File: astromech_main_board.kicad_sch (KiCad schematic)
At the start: 0 parts

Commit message: added blocks
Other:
- added sheet ESP32 (ESP32.kicad_sch)
- added sheet io_expander (io_expander.kicad_sch)
- added sheet io_protection (io_protection.kicad_sch)
- added sheet power_protection (power_protection.kicad_sch)
- added sheet voltage_monitoring (voltage_monitoring.kicad_sch)
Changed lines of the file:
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@@
 	(generator_version "8.0")
 	(paper "A4")
+	(sheet
+		(at 172.72 121.92)
+		(size 34.29 27.94)
+		(fields_autoplaced yes)
+		(stroke
+			(width 0.1524)
+			(type solid)
+		)
+		(fill
+			(color 0 0 0 0.0000)
+		)
+		(property "Sheetname" "io_protection"
+			(at 172.72 121.2084 0)
+			(effects
+				(font
+					(size 1.27 1.27)
+				)
+				(justify left bottom)
+			)
+		)
+		(property "Sheetfile" "io_protection.kicad_sch"
+			(at 172.72 150.4446 0)
+			(effects
+				(font
+					(size 1.27 1.27)
+				)
+				(justify left top)
+			)
+		)
+		(instances
+			(project "astromech_main_board"
+				(path "/3ed70c37-1dc6-4761-9813-fca49ce12494"
+					(page "6")
+				)
+			)
+		)
+	)
+	(sheet
+		(at 115.57 128.27)
+		(size 39.37 35.56)
+		(fields_autoplaced yes)
+		(stroke
+			(width 0.1524)
+			(type solid)
+		)
+		(fill
+			(color 0 0 0 0.0000)
+		)
+		(property "Sheetname" "io_expander"
+			(at 115.57 127.5584 0)
+			(effects
+				(font
+					(size 1.27 1.27)
+				)
+				(justify left bottom)
+			)
+		)
+		(property "Sheetfile" "io_expander.kicad_sch"
+			(at 115.57 164.4146 0)
+			(effects
+				(font
+					(size 1.27 1.27)
+				)
+				(justify left top)
+			)
+		)
+		(instances
+			(project "astromech_main_board"
+				(path "/3ed70c37-1dc6-4761-9813-fca49ce12494"
+					(page "5")
+				)
+			)
+		)
+	)
+	(sheet
+		(at 45.72 109.22)
+		(size 35.56 30.48)
+		(fields_autoplaced yes)
+		(stroke
+			(width 0.1524)
+			(type solid)
+		)
+		(fill
+			(color 0 0 0 0.0000)
+		)
+		(property "Sheetname" "power_protection"
+			(at 45.72 108.5084 0)
+			(effects
+				(font
+					(size 1.27 1.27)
+				)
+				(justify left bottom)
+			)
+		)
+		(property "Sheetfile" "power_protection.kicad_sch"
+			(at 45.72 140.2846 0)
+			(effects
+				(font
+					(size 1.27 1.27)
+				)
+				(justify left top)
+			)
+		)
+		(instances
+			(project "astromech_main_board"
+				(path "/3ed70c37-1dc6-4761-9813-fca49ce12494"
+					(page "4")
+				)
+			)
+		)
+	)
+	(sheet
+		(at 125.73 66.04)
+		(size 34.29 48.26)
+		(fields_autoplaced yes)
+		(stroke
+			(width 0.1524)
+			(type solid)
+		)
+		(fill
+			(color 0 0 0 0.0000)
+		)
+		(property "Sheetname" "ESP32"
+			(at 125.73 65.3284 0)
+			(effects
+				(font
+					(size 1.27 1.27)
+				)
+				(justify left bottom)
+			)
+		)
+		(property "Sheetfile" "ESP32.kicad_sch"
+			(at 125.73 114.8846 0)
+			(effects
+				(font
+					(size 1.27 1.27)
+				)
+				(justify left top)
+			)
+		)
+		(instances
+			(project "astromech_main_board"
+				(path "/3ed70c37-1dc6-4761-9813-fca49ce12494"
+					(page "2")
+				)
+			)
+		)
+	)
+	(sheet
+		(at 45.72 55.88)
+		(size 30.48 30.48)
+		(fields_autoplaced yes)
+		(stroke
+			(width 0.1524)
+			(type solid)
+		)
+		(fill
+			(color 0 0 0 0.0000)
+		)
+		(property "Sheetname" "voltage_monitoring"
+			(at 45.72 55.1684 0)
+			(effects
+				(font
+					(size 1.27 1.27)
+				)
+				(justify left bottom)
+			)
+		)
+		(property "Sheetfile" "voltage_monitoring.kicad_sch"
+			(at 45.72 86.9446 0)
+			(effects
+				(font
+					(size 1.27 1.27)
+				)
+				(justify left top)
+			)
+		)
+		(instances
+			(project "astromech_main_board"
+				(path "/3ed70c37-1dc6-4761-9813-fca49ce12494"
+					(page "3")
+				)
+			)
+		)
+	)
 	(sheet_instances
 		(path "/"

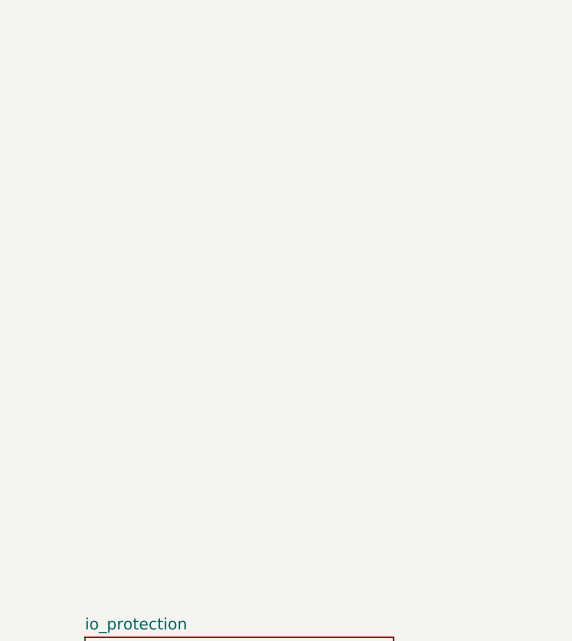
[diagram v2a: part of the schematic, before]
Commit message: added hw encoder
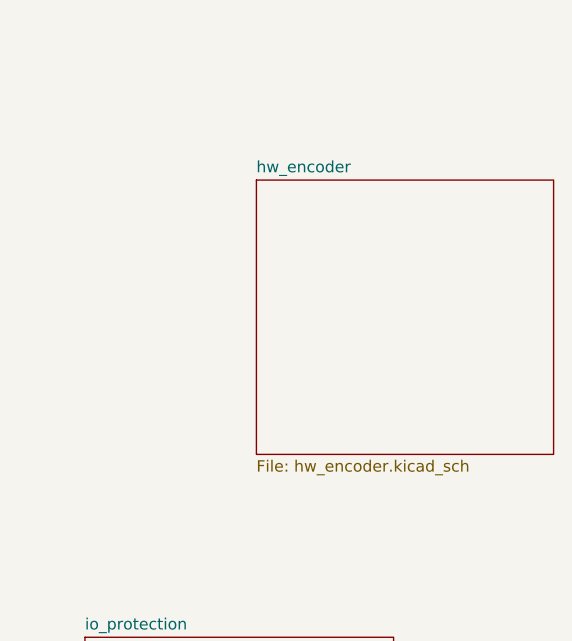
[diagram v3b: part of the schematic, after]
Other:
- added sheet hw_encoder (hw_encoder.kicad_sch)
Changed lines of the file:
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@@
 	(paper "A4")
+	(sheet
+		(at 191.77 71.12)
+		(size 33.02 30.48)
+		(fields_autoplaced yes)
+		(stroke
+			(width 0.1524)
+			(type solid)
+		)
+		(fill
+			(color 0 0 0 0.0000)
+		)
+		(property "Sheetname" "hw_encoder"
+			(at 191.77 70.4084 0)
+			(effects
+				(font
+					(size 1.27 1.27)
+				)
+				(justify left bottom)
+			)
+		)
+		(property "Sheetfile" "hw_encoder.kicad_sch"
+			(at 191.77 102.1846 0)
+			(effects
+				(font
+					(size 1.27 1.27)
+				)
+				(justify left top)
+			)
+		)
+		(instances
+			(project "astromech_main_board"
+				(path "/3ed70c37-1dc6-4761-9813-fca49ce12494"
+					(page "7")
+				)
+			)
+		)
+	)
 	(sheet
 		(at 172.72 121.92)

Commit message: moved power protection
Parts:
- added C1, C3: 0.1u, symbol Device:C_Polarized_Small
- added C2: C_Polarized, symbol Device:C_Polarized
- added F1, F2: ??A, symbol Device:Fuse_Small
- added J1, J2: Screw_Terminal_01x02, symbol Connector:Screw_Terminal_01x02
- added JP10, JP11, JP9: SolderJumper_3_Open, symbol Jumper:SolderJumper_3_Open
- added U7, U9: NCP1117-5.0_TO252, Package_TO_SOT_SMD:TO-252-2, symbol Regulator_Linear:NCP1117-5.0_TO252
- added U8: NCP1117-3.3_SOT223, Package_TO_SOT_SMD:SOT-223-3_TabPin2, symbol Regulator_Linear:NCP1117-3.3_SOT223
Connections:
- new net: JP10.1 (A), U7.2 (VO)
- new net: JP10.3 (B), U7.3 (VI)
- new net: F2.1, J2.1 (Pin_1)
- new net: JP11.3 (B), U8.3 (VI)
- new net: JP9.3 (B), U9.3 (VI)
- new net: F1.1, J1.1 (Pin_1)
- new net 3V3_IN: C3.1, F1.2, JP11.2 (C)
- new net 3V3_REG: JP11.1 (A), U8.2 (VO)
- new net 5V_IN: C1.1, F2.2, JP9.2 (C)
- new net 5V_REG: JP9.1 (A), U9.2 (VO)
- new net GND: C1.2, C2.2, C3.2, J1.2 (Pin_2), J2.2 (Pin_2), U7.1 (GND), U8.1 (GND), U9.1 (GND)
- new net VCC: C2.1, JP10.2 (C)
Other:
- removed sheet power_protection
- sheet ESP32 ports: added 3V3_IN, 5Vin, DPAD_CENTER, DPAD_COM, DPAD_DOWN, DPAD_LEFT, DPAD_RIGHT, DPAD_UP, ENC_HEAD_CS, ENC_HEAD_PICO, ENC_HEAD_POCI, ENC_HEAD_SCK, ENC_LEFT_CS, ENC_LEFT_PICO, ENC_LEFT_POCI, ENC_LEFT_SCK, ENC_RIGHT_CS, ENC_RIGHT_PICO, ENC_RIGHT_POCI, ENC_RIGHT_SCK, GND, I2C_SCL, I2C_SDA, PWM_HEAD, PWM_LEFT, PWM_RIGHT, SCREEN_CS, SCREEN_PICO, SCREEN_POCI, SCREEN_SCK, UART_GP_RX, UART_GP_TX, UART_RC_RX, UART_RC_TX, UI_HEARTBEAT, UI_POWER; removed none
- note added: "5.0 Voltage Input"
- note added: "Non-Regualted Voltage"
- note added: "Output Voltage"
- note added: "Regulated Voltage"

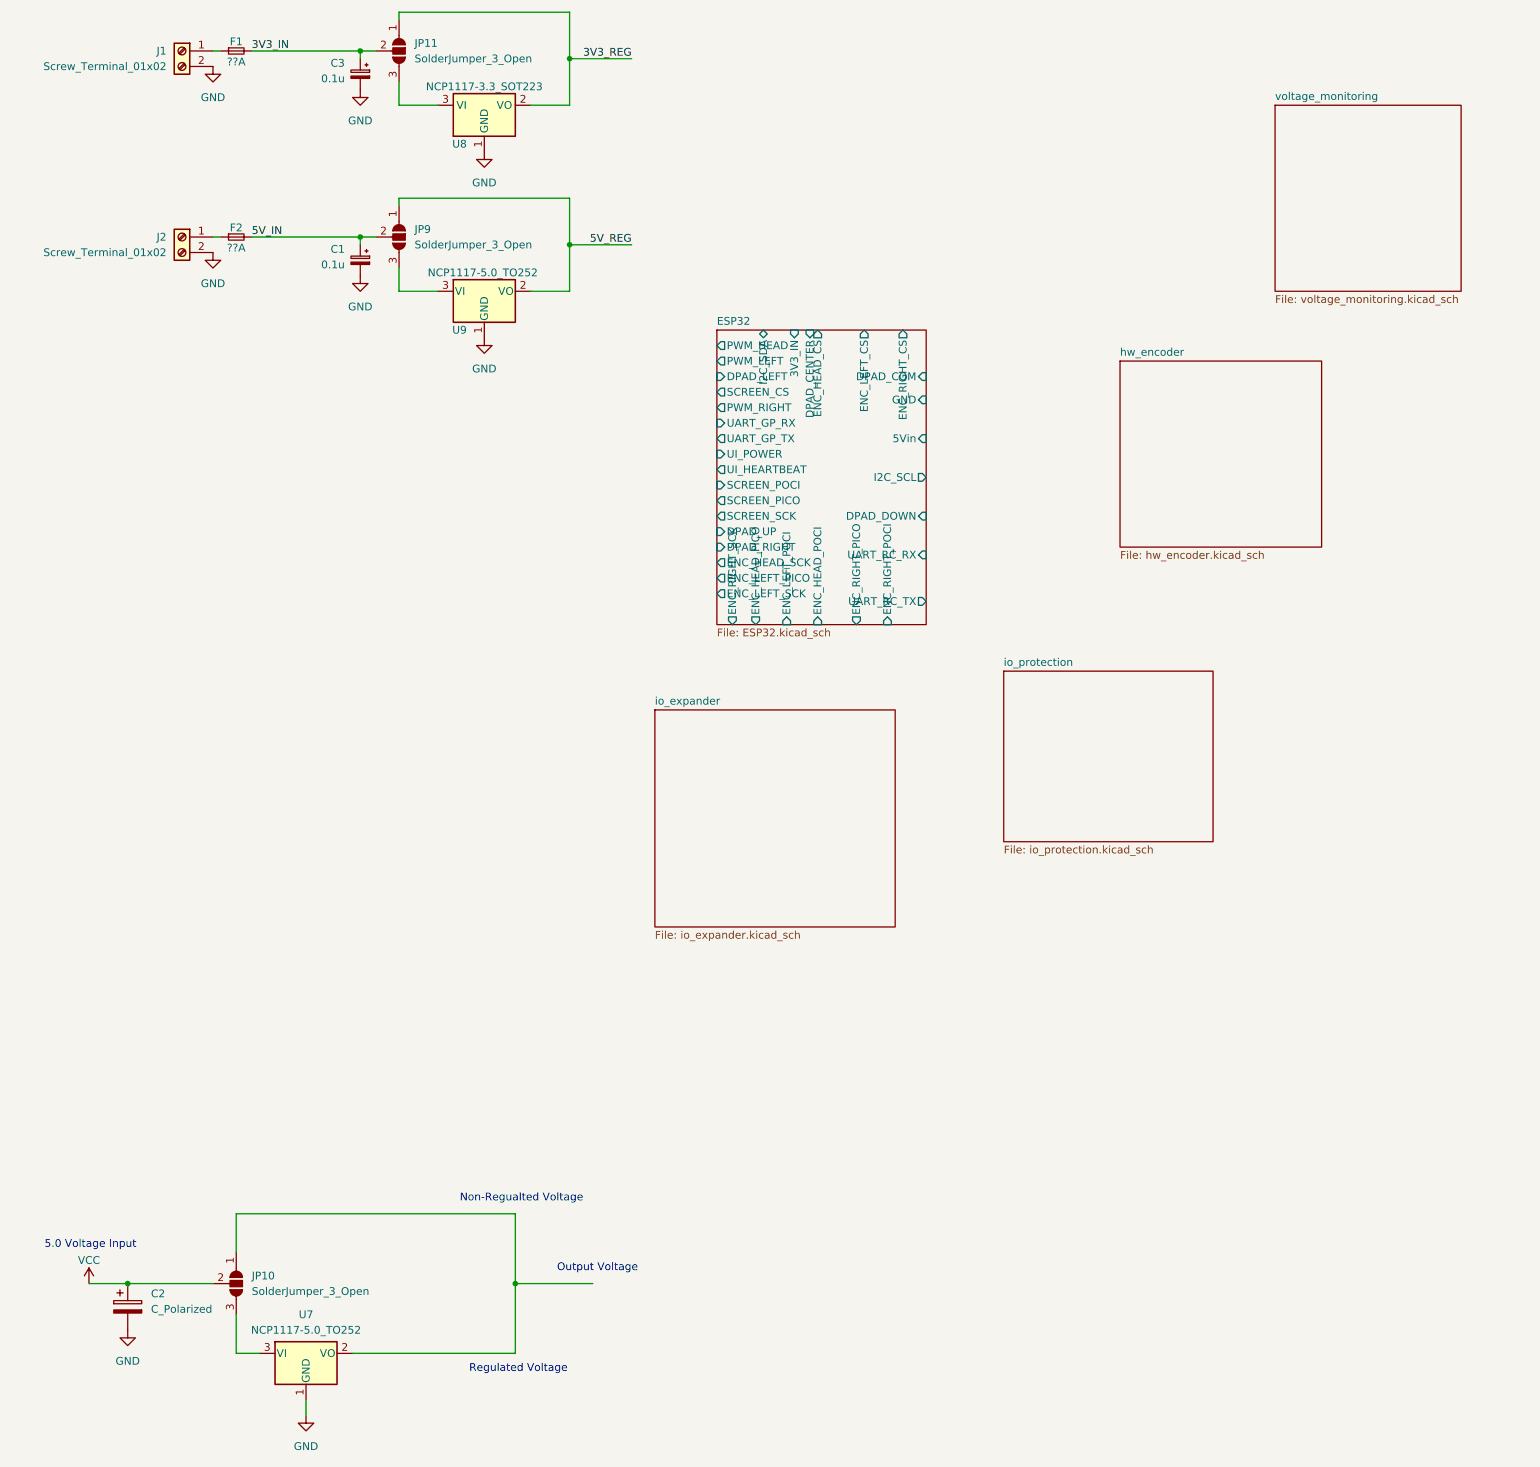
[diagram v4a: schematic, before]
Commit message: moved voltage monitoring
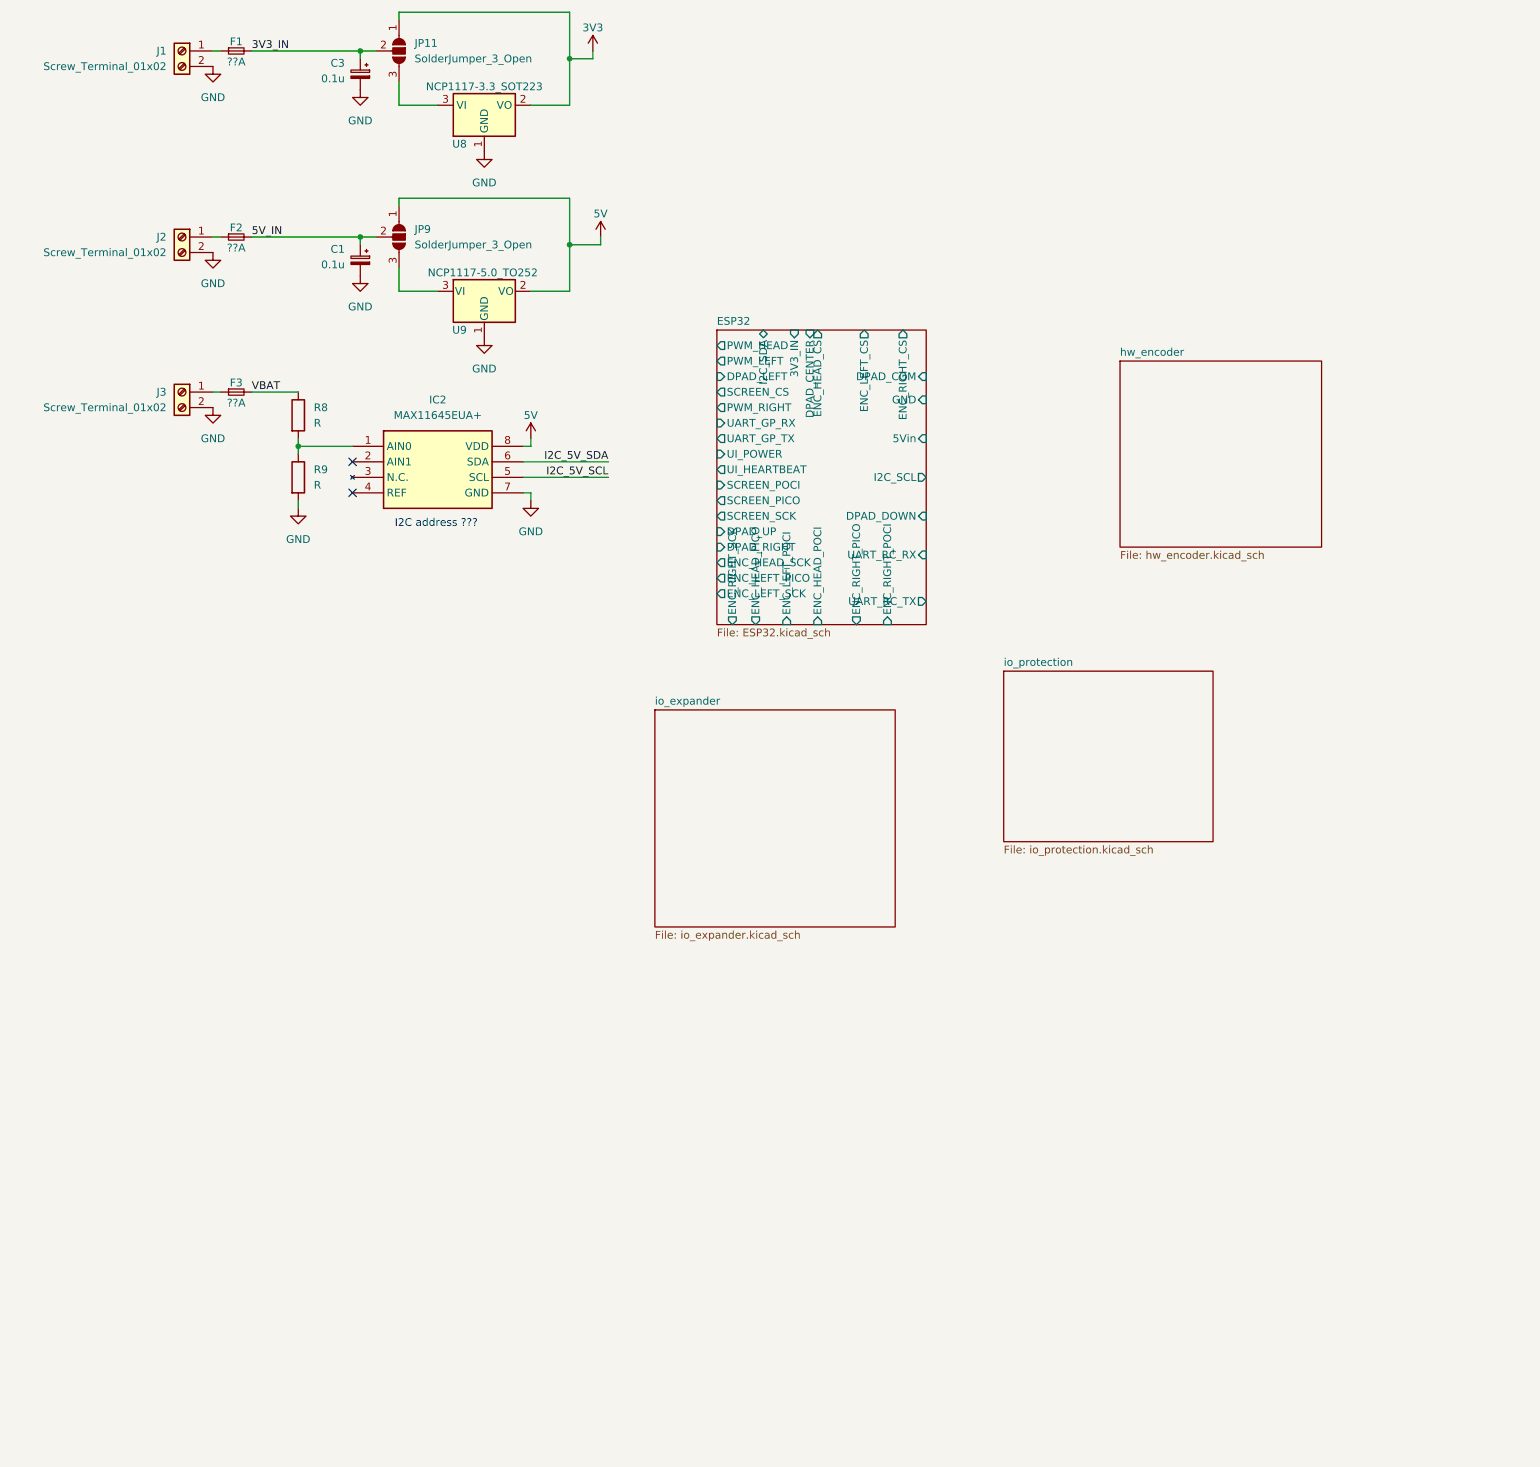
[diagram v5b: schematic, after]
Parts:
- removed C2: C_Polarized, symbol Device:C_Polarized
- removed JP10: SolderJumper_3_Open, symbol Jumper:SolderJumper_3_Open
- removed U7: NCP1117-5.0_TO252, Package_TO_SOT_SMD:TO-252-2, symbol Regulator_Linear:NCP1117-5.0_TO252
- added F3: ??A, symbol Device:Fuse_Small
- added IC2: MAX11645EUA+, SOP65P490X111-8N, symbol MAX11645EUA+:MAX11645EUA+
- added J3: Screw_Terminal_01x02, symbol Connector:Screw_Terminal_01x02
- added R8, R9: R, symbol Device:R
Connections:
- net GND: now also IC2.7 (GND), J3.2 (Pin_2), R9.2
- net 3V3_REG renamed 3V3
- net 5V_REG renamed 5V
- net 5V: now also IC2.8 (VDD)
- new net: F3.1, J3.1 (Pin_1)
- new net: IC2.1 (AIN0), R8.2, R9.1
- new net I2C_5V_SCL: IC2.5 (SCL)
- new net I2C_5V_SDA: IC2.6 (SDA)
- new net VBAT: F3.2, R8.1
- no-connect marks 0 -> 2
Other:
- removed sheet voltage_monitoring
- note added: "I2C address ???"
- note removed: "5.0 Voltage Input"
- note removed: "Non-Regualted Voltage"
- note removed: "Output Voltage"
- note removed: "Regulated Voltage"
